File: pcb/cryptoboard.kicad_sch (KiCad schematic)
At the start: 36 parts, among them J1 USB_A, J2 BOOT, J3 SWD, J4 USR_LEFT, J5 USR_RIGHT, J6 Conn_01x04, SW1 SW_Push, U2 LM317_SOT-223-3.3V, U3 STM32F107RBTx, Y1 Crystal

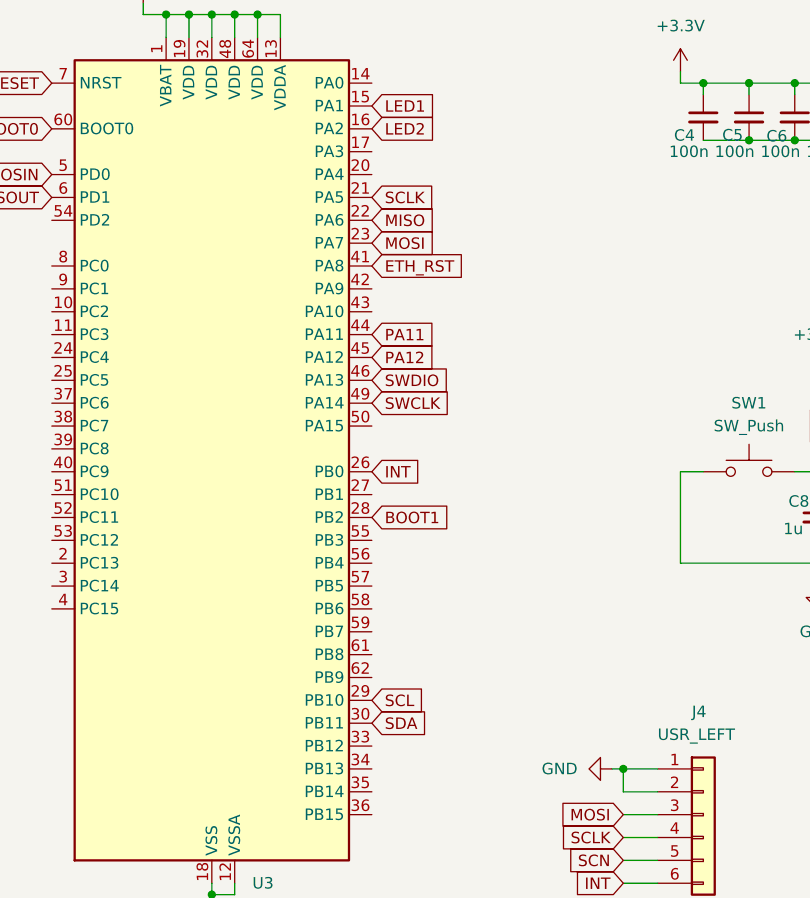
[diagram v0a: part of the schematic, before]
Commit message: add spi and I2c
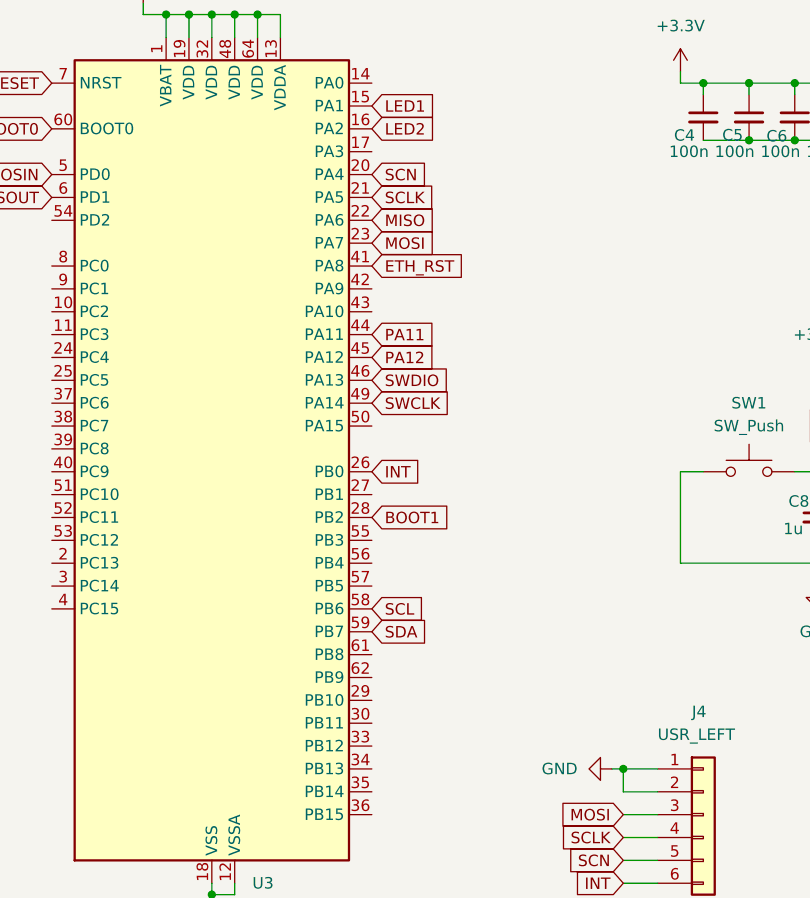
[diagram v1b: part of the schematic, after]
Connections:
- net SCL: now also U3.58 (PB6); no longer U3.29 (PB10)
- net SCN: now also U3.20 (PA4)
- net SDA: now also U3.59 (PB7); no longer U3.30 (PB11)
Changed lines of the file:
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@@
     (stroke (width 0) (type default))
   )
+  (global_label "SCN" (shape input) (at 121.92 73.66 0) (fields_autoplaced)
+    (effects (font (size 1.27 1.27)) (justify left))
+    (property "Intersheetrefs" "${INTERSHEET_REFS}" (at 128.6358 73.66 0)
+      (effects (font (size 1.27 1.27)) (justify left) hide)
+    )
+  )
   (global_label "SCN" (shape input) (at 149.86 149.86 180) (fields_autoplaced)
     (effects (font (size 1.27 1.27)) (justify right))
@@
     )
   )
+  (global_label "SCL" (shape input) (at 121.92 121.92 0) (fields_autoplaced)
+    (effects (font (size 1.27 1.27)) (justify left))
+    (property "Intersheetrefs" "${INTERSHEET_REFS}" (at 128.3334 121.92 0)
+      (effects (font (size 1.27 1.27)) (justify left) hide)
+    )
+  )
   (global_label "BOOT1" (shape input) (at 121.92 111.76 0) (fields_autoplaced)
     (effects (font (size 1.27 1.27)) (justify left))
@@
     )
   )
+  (global_label "SDA" (shape input) (at 121.92 124.46 0) (fields_autoplaced)
+    (effects (font (size 1.27 1.27)) (justify left))
+    (property "Intersheetrefs" "${INTERSHEET_REFS}" (at 128.3939 124.46 0)
+      (effects (font (size 1.27 1.27)) (justify left) hide)
+    )
+  )
   (global_label "OSOUT" (shape input) (at 102.87 182.88 180) (fields_autoplaced)
     (effects (font (size 1.27 1.27)) (justify right))
@@
     )
   )
-  (global_label "SCL" (shape input) (at 121.92 132.08 0) (fields_autoplaced)
-    (effects (font (size 1.27 1.27)) (justify left))
-    (property "Intersheetrefs" "${INTERSHEET_REFS}" (at 128.3334 132.08 0)
-      (effects (font (size 1.27 1.27)) (justify left) hide)
-    )
-  )
   (global_label "RESET" (shape input) (at 177.8 106.68 0) (fields_autoplaced)
     (effects (font (size 1.27 1.27)) (justify left))
@@
       (effects (font (size 1.27 1.27)) (justify left) hide)
     )
-  )
-  (global_label "SDA" (shape input) (at 121.92 134.62 0) (fields_autoplaced)
-    (effects (font (size 1.27 1.27)) (justify left))
-    (property "Intersheetrefs" "${INTERSHEET_REFS}" (at 128.3939 134.62 0)
-      (effects (font (size 1.27 1.27)) (justify left) hide)
-    )
